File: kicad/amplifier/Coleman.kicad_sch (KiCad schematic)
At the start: 26 parts, among them Q10 STP55NF06L, Q11 STP55NF06L, Q12 STP55NF06L, Q9 STP55NF06L, U5 TL431, U6 TL431

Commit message: up
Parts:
- removed TH1: CL-110, Varistor:RV_Disc_D12mm_W4.3mm_P7.5mm, symbol Device:Thermistor_NTC
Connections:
- net +RAW_DC: now reaches C8.1, Q10.1 (D), Q9.1 (D), R28.2, R29.2
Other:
- note removed: "from SMPS"
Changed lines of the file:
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@@
     (stroke (width 0) (type default))
   )
-  (wire (pts (xy 100.33 111.76) (xy 119.38 111.76))
-    (stroke (width 0) (type default))
-  )
-  (wire (pts (xy 100.33 82.55) (xy 105.41 82.55))
+  (wire (pts (xy 110.49 111.76) (xy 119.38 111.76))
+    (stroke (width 0) (type default))
+  )
+  (wire (pts (xy 110.49 82.55) (xy 119.38 82.55))
     (stroke (width 0) (type default))
   )
@@
   )
   (wire (pts (xy 173.99 82.55) (xy 179.07 82.55))
-    (stroke (width 0) (type default))
-  )
-  (wire (pts (xy 113.03 82.55) (xy 119.38 82.55))
     (stroke (width 0) (type default))
   )
@@
     (fill (type none))
   )
-  (text "from SMPS" (at 87.63 86.36 0)
-    (effects (font (size 1.27 1.27)) (justify left bottom))
-  )
   (text "CCS" (at 168.91 73.66 0)
     (effects (font (size 1.27 1.27)) (justify left bottom))
@@
     (effects (font (size 1.27 1.27)) (justify left))
   )
-  (hierarchical_label "GND" (shape passive) (at 100.33 111.76 180) (fields_autoplaced)
+  (hierarchical_label "GND" (shape passive) (at 110.49 111.76 180) (fields_autoplaced)
     (effects (font (size 1.27 1.27)) (justify right))
   )
@@
     (effects (font (size 1.27 1.27)) (justify left))
   )
-  (hierarchical_label "+RAW_15VDC" (shape passive) (at 100.33 82.55 180) (fields_autoplaced)
+  (hierarchical_label "+RAW_DC" (shape passive) (at 110.49 82.55 180) (fields_autoplaced)
     (effects (font (size 1.27 1.27)) (justify right))
   )
@@
         )
       )
-    )
-  )
-  (symbol (lib_id "Device:Thermistor_NTC") (at 109.22 82.55 90) (unit 1)
-    (in_bom yes) (on_board yes) (dnp no) (fields_autoplaced)
-    (property "Reference" "TH1" (at 109.5375 76.2 90)
-      (effects (font (size 1.27 1.27)))
-    )
-    (property "Value" "CL-110" (at 109.5375 78.74 90)
-      (effects (font (size 1.27 1.27)))
-    )
-    (property "Footprint" "Varistor:RV_Disc_D12mm_W4.3mm_P7.5mm" (at 107.95 82.55 0)
-      (effects (font (size 1.27 1.27)) hide)
-    )
-    (property "Datasheet" "~" (at 107.95 82.55 0)
-      (effects (font (size 1.27 1.27)) hide)
-    )
-    (pin "2")
-    (pin "1")
-    (instances
-      (project "OSDEHA_AMP"
-        (path "/59cc4414-299b-49db-9f9a-b06f69a12073/c1ba13e4-6fba-4c1a-9fa1-489c0cbbcd0f"
-          (reference "TH1") (unit 1)
-        )
-      )

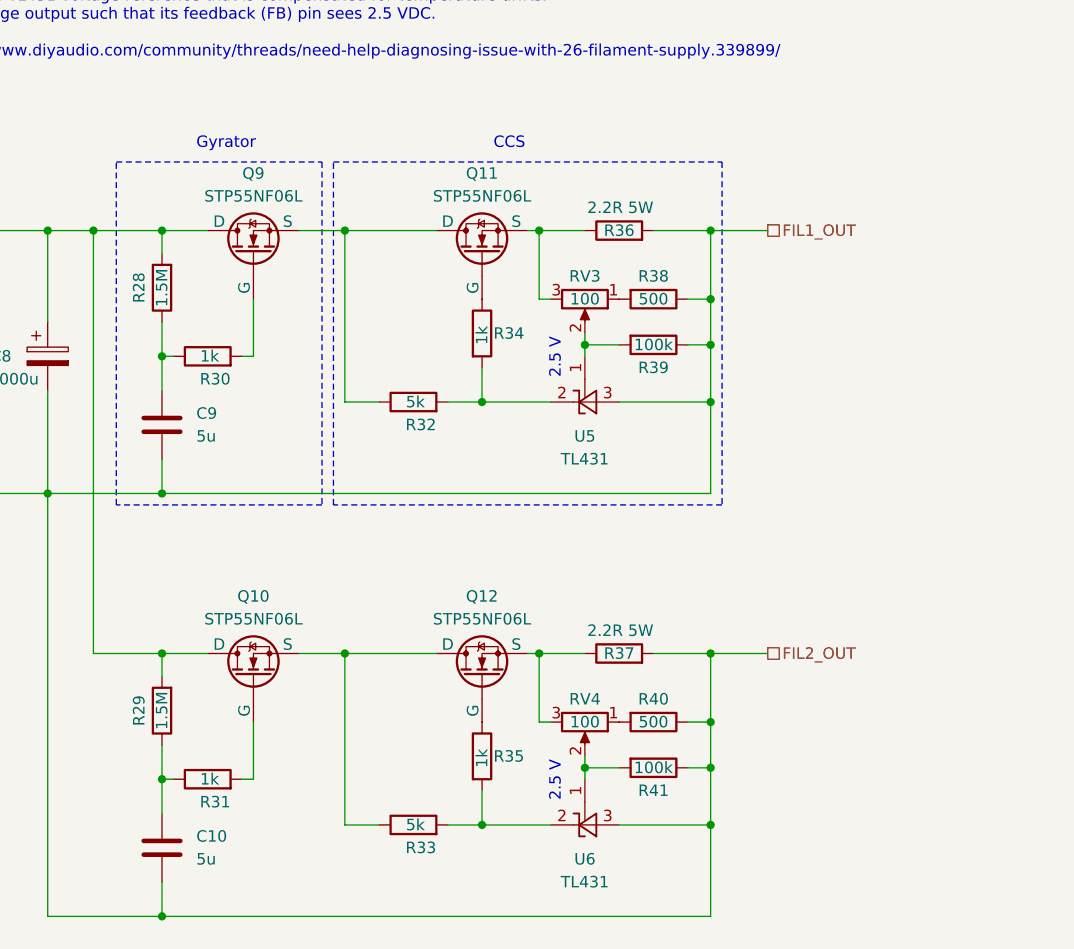
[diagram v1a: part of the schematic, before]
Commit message: fixed error in filament supply
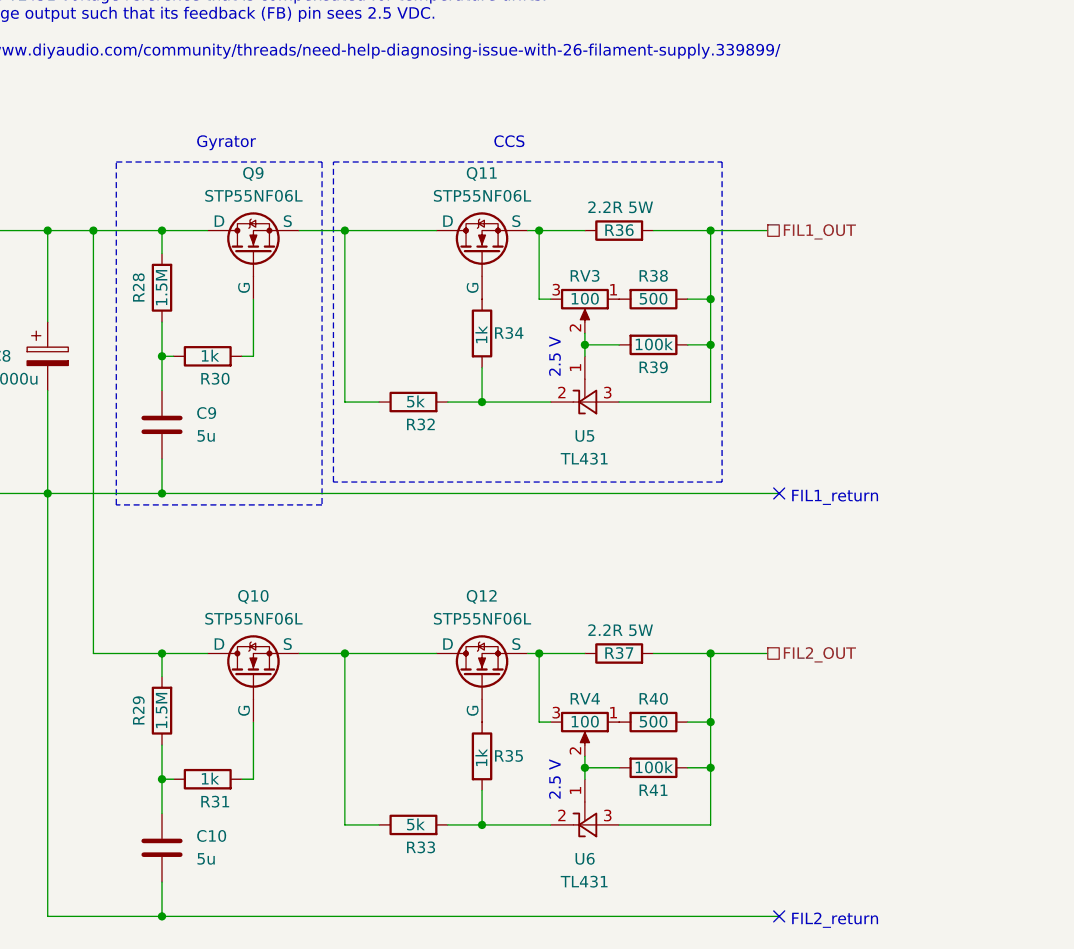
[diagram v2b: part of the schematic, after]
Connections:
- net FIL1_OUT: no longer C10.2, C8.2, C9.2, R37.2, R40.1, R41.1, U6.3 (A)
- new net FIL2_OUT: R37.2, R40.1, R41.1, U6.3 (A)
- new net GND: C10.2, C8.2, C9.2
- no-connect marks 0 -> 2
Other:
- note added: "FIL1_return"
- note added: "FIL2_return"
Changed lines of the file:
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@@
 (kicad_sch (version 20230121) (generator eeschema)
   (paper "A4")
-  (junction (at 193.04 101.6) (diameter 0) (color 0 0 0 0)
-  )
   (junction (at 132.08 129.54) (diameter 0) (color 0 0 0 0)
   )
@@
   (junction (at 193.04 137.16) (diameter 0) (color 0 0 0 0)
   )
-  (junction (at 193.04 148.59) (diameter 0) (color 0 0 0 0)
-  )
   (junction (at 179.07 142.24) (diameter 0) (color 0 0 0 0)
   )
@@
   (junction (at 119.38 111.76) (diameter 0) (color 0 0 0 0)
   )
+  (junction (at 132.08 158.75) (diameter 0) (color 0 0 0 0)
+  )
   (junction (at 173.99 82.55) (diameter 0) (color 0 0 0 0)
   )
@@
   (junction (at 132.08 111.76) (diameter 0) (color 0 0 0 0)
   )
-  (junction (at 132.08 158.75) (diameter 0) (color 0 0 0 0)
-  )
+  (no_connect (at 200.66 158.75))
+  (no_connect (at 200.66 111.76))
   (wire (pts (xy 175.26 90.17) (xy 173.99 90.17))
     (stroke (width 0) (type default))
@@
     (stroke (width 0) (type default))
   )
-  (wire (pts (xy 193.04 158.75) (xy 132.08 158.75))
-    (stroke (width 0) (type default))
-  )
   (wire (pts (xy 142.24 137.16) (xy 142.24 143.51))
     (stroke (width 0) (type default))
@@
     (stroke (width 0) (type default))
   )
-  (wire (pts (xy 193.04 148.59) (xy 193.04 158.75))
-    (stroke (width 0) (type default))
-  )
   (wire (pts (xy 179.07 142.24) (xy 179.07 140.97))
     (stroke (width 0) (type default))
@@
     (stroke (width 0) (type default))
   )
+  (wire (pts (xy 132.08 158.75) (xy 200.66 158.75))
+    (stroke (width 0) (type default))
+  )
   (wire (pts (xy 124.46 82.55) (xy 132.08 82.55))
     (stroke (width 0) (type default))
@@
     (stroke (width 0) (type default))
   )
-  (wire (pts (xy 193.04 111.76) (xy 132.08 111.76))
+  (wire (pts (xy 132.08 111.76) (xy 200.66 111.76))
     (stroke (width 0) (type default))
   )
@@
     (stroke (width 0) (type default))
   )
-  (wire (pts (xy 193.04 101.6) (xy 193.04 111.76))
-    (stroke (width 0) (type default))
-  )
   (wire (pts (xy 119.38 92.71) (xy 119.38 82.55))
     (stroke (width 0) (type default))
@@
     (stroke (width 0) (type default))
   )
-  (rectangle (start 151.13 74.93) (end 194.31 113.03)
+  (rectangle (start 151.13 74.93) (end 194.31 110.49)
     (stroke (width 0) (type dash))
     (fill (type none))
@@
     (fill (type none))
   )
+  (text "FIL1_return" (at 201.93 113.03 0)
+    (effects (font (size 1.27 1.27)) (justify left bottom))
+  )
   (text "CCS" (at 168.91 73.66 0)
     (effects (font (size 1.27 1.27)) (justify left bottom))
@@
     (effects (font (size 1.27 1.27)) (justify left bottom))
   )
+  (text "FIL2_return" (at 201.93 160.02 0)
+    (effects (font (size 1.27 1.27)) (justify left bottom))
+  )

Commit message: notes on DHT filament CCS
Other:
- note added: "New attempt to make things easier: Take a look at the last schematic here: https://www.mvaudiolabs.com/tubes/the-taming-of-the-dht/ Then split this up in a common raw-DC supply and ripple filter: - ripple filter DC+ output connects to GND (or B- in the OSDEHA) - one side of each DHT filament connects to GND (or B-) as well. - the other side of each filament connects to it's own CCS as shown on th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"
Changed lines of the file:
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@@
     (effects (font (size 1.27 1.27)) (justify left bottom))
+  )
+  (text "New attempt to make things easier:\nTake a look at the last schematic here:\nhttps://www.mvaudiolabs.com/tubes/the-taming-of-the-dht/\n\nThen split this up in a common raw-DC supply and ripple filter:\n- ripple filter DC+ output connects to GND (or B- in the OSDEHA)\n- one side of each DHT filament connects to GND (or B-) as well.\n- the other side of each filament connects to it's own CCS as shown on the website\n\nWhat about thermal drift? Adjustment of the heater current will take a bit of patience to get the desired filament voltage. Maybe an NTC/PTC connected to the base of the diff-amp BC550 will help. "
+    (at 20.32 62.23 0)
+    (effects (font (size 3 3) (thickness 0.3) bold) (justify left bottom))
   )
   (text "CCS" (at 168.91 73.66 0)
@@
   )
   (text "Inspired by Rod Coleman DHT Filament Regulator:\n(for discussion: https://wtfamps.com/2018/10/03/diy-dht-filament-strategies)\n- Filament driven by high-impedance source (CCS)\n- Gyrator for DC voltage smoothing\n\nPublished versions of Coleman DHT Filament regulator cannot be operated from same raw DC supply\nbecause the Gyrator and CCS sit on opposite ends of each filament,\nand one end of each filament is connected to B-, so the corresponding outputs of each regulator are connected to each other.\n\nAfter discussion with Rod Coleman (PM diyAudio), the CCS was moved to the same side as the gyrator.\nCCS must be the \"driver\" for the filament, so it sits between the filament and the gyrator.\n\nThe CCS uses an adjustable TL431 voltage reference that is compensated for temperature drifts.\nThe LM431 adjusts its voltage output such that its feedback (FB) pin sees 2.5 VDC.\n\nCircuit inspired by https://www.diyaudio.com/community/threads/need-help-diagnosing-issue-with-26-filament-supply.339899/"
-    (at 90.17 63.5 0)
+    (at 231.14 121.92 0)
     (effects (font (size 1.27 1.27)) (justify left bottom))
   )

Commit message: up
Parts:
- R28, R29, R30, R31, R32, R33, R34, R35, R38, R39, R40, R41: footprint (none) -> Resistor_THT:R_Axial_DIN0207_L6.3mm_D2.5mm_P10.16mm_Horizontal
- RV3, RV4: footprint (none) -> Potentiometer_THT:Potentiometer_Bourns_3296W_Vertical
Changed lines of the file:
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@@
       (effects (font (size 1.27 1.27)))
     )
-    (property "Footprint" "" (at 186.69 93.472 90)
+    (property "Footprint" "Resistor_THT:R_Axial_DIN0207_L6.3mm_D2.5mm_P10.16mm_Horizontal" (at 186.69 93.472 90)
       (effects (font (size 1.27 1.27)) hide)
     )
@@
       (effects (font (size 1.27 1.27)) (justify left))
     )
-    (property "Footprint" "" (at 160.02 103.378 90)
+    (property "Footprint" "Resistor_THT:R_Axial_DIN0207_L6.3mm_D2.5mm_P10.16mm_Horizontal" (at 160.02 103.378 90)
       (effects (font (size 1.27 1.27)) hide)
     )
@@
       (effects (font (size 1.27 1.27)) (justify left))
     )
-    (property "Footprint" "" (at 160.02 150.368 90)
+    (property "Footprint" "Resistor_THT:R_Axial_DIN0207_L6.3mm_D2.5mm_P10.16mm_Horizontal" (at 160.02 150.368 90)
       (effects (font (size 1.27 1.27)) hide)
     )
@@
       (effects (font (size 1.27 1.27)) (justify left))
     )
-    (property "Footprint" "" (at 137.16 98.298 90)
+    (property "Footprint" "Resistor_THT:R_Axial_DIN0207_L6.3mm_D2.5mm_P10.16mm_Horizontal" (at 137.16 98.298 90)
       (effects (font (size 1.27 1.27)) hide)
     )
@@
       (effects (font (size 1.27 1.27)))
     )
-    (property "Footprint" "" (at 179.07 137.16 0)
+    (property "Footprint" "Potentiometer_THT:Potentiometer_Bourns_3296W_Vertical" (at 179.07 137.16 0)
       (effects (font (size 1.27 1.27)) hide)
     )
@@
       (effects (font (size 1.27 1.27)))
     )
-    (property "Footprint" "" (at 186.69 135.382 90)
+    (property "Footprint" "Resistor_THT:R_Axial_DIN0207_L6.3mm_D2.5mm_P10.16mm_Horizontal" (at 186.69 135.382 90)
       (effects (font (size 1.27 1.27)) hide)
     )
@@
       (effects (font (size 1.27 1.27)) (justify left))
     )
-    (property "Footprint" "" (at 165.862 93.98 90)
+    (property "Footprint" "Resistor_THT:R_Axial_DIN0207_L6.3mm_D2.5mm_P10.16mm_Horizontal" (at 165.862 93.98 90)
       (effects (font (size 1.27 1.27)) hide)
     )
@@
       (effects (font (size 1.27 1.27)) (justify left))
     )
-    (property "Footprint" "" (at 137.16 145.288 90)
+    (property "Footprint" "Resistor_THT:R_Axial_DIN0207_L6.3mm_D2.5mm_P10.16mm_Horizontal" (at 137.16 145.288 90)
       (effects (font (size 1.27 1.27)) hide)
     )
@@
       (effects (font (size 1.27 1.27)))
     )
-    (property "Footprint" "" (at 186.69 88.392 90)
+    (property "Footprint" "Resistor_THT:R_Axial_DIN0207_L6.3mm_D2.5mm_P10.16mm_Horizontal" (at 186.69 88.392 90)
       (effects (font (size 1.27 1.27)) hide)
     )
@@
       (effects (font (size 1.27 1.27)))
     )
-    (property "Footprint" "" (at 179.07 90.17 0)
+    (property "Footprint" "Potentiometer_THT:Potentiometer_Bourns_3296W_Vertical" (at 179.07 90.17 0)
       (effects (font (size 1.27 1.27)) hide)
     )
@@
       (effects (font (size 1.27 1.27)))
     )
-    (property "Footprint" "" (at 133.858 88.9 90)
+    (property "Footprint" "Resistor_THT:R_Axial_DIN0207_L6.3mm_D2.5mm_P10.16mm_Horizontal" (at 133.858 88.9 90)
       (effects (font (size 1.27 1.27)) hide)
     )
@@
       (effects (font (size 1.27 1.27)))
     )
-    (property "Footprint" "" (at 186.69 140.462 90)
+    (property "Footprint" "Resistor_THT:R_Axial_DIN0207_L6.3mm_D2.5mm_P10.16mm_Horizontal" (at 186.69 140.462 90)
       (effects (font (size 1.27 1.27)) hide)
     )
@@
       (effects (font (size 1.27 1.27)))
     )
-    (property "Footprint" "" (at 133.858 135.89 90)
+    (property "Footprint" "Resistor_THT:R_Axial_DIN0207_L6.3mm_D2.5mm_P10.16mm_Horizontal" (at 133.858 135.89 90)
       (effects (font (size 1.27 1.27)) hide)
     )
@@
       (effects (font (size 1.27 1.27)) (justify left))
     )
-    (property "Footprint" "" (at 165.862 140.97 90)
-      (effects (font (size 1.27 1.27)) hide)
-    )
+    (property "Footprint" "Resistor_THT:R_Axial_DIN0207_L6.3mm_D2.5mm_P10.16mm_Horizontal" (at 165.862 140.97 90)
+      (effects (font (size 1.27 1.27)) hide)
+    )

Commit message: up
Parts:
- R36, R37: footprint (none) -> Resistor_THT:R_Axial_Power_L25.0mm_W9.0mm_P30.48mm
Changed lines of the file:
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@@
       (effects (font (size 1.27 1.27)) (justify left))
     )
-    (property "Footprint" "" (at 182.88 131.318 90)
+    (property "Footprint" "Resistor_THT:R_Axial_Power_L25.0mm_W9.0mm_P30.48mm" (at 182.88 131.318 90)
       (effects (font (size 1.27 1.27)) hide)
     )
@@
       (effects (font (size 1.27 1.27)) (justify left))
     )
-    (property "Footprint" "" (at 182.88 84.328 90)
-      (effects (font (size 1.27 1.27)) hide)
-    )
+    (property "Footprint" "Resistor_THT:R_Axial_Power_L25.0mm_W9.0mm_P30.48mm" (at 182.88 84.328 90)
+      (effects (font (size 1.27 1.27)) hide)
+    )
